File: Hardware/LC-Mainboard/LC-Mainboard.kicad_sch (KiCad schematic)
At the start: 15 parts

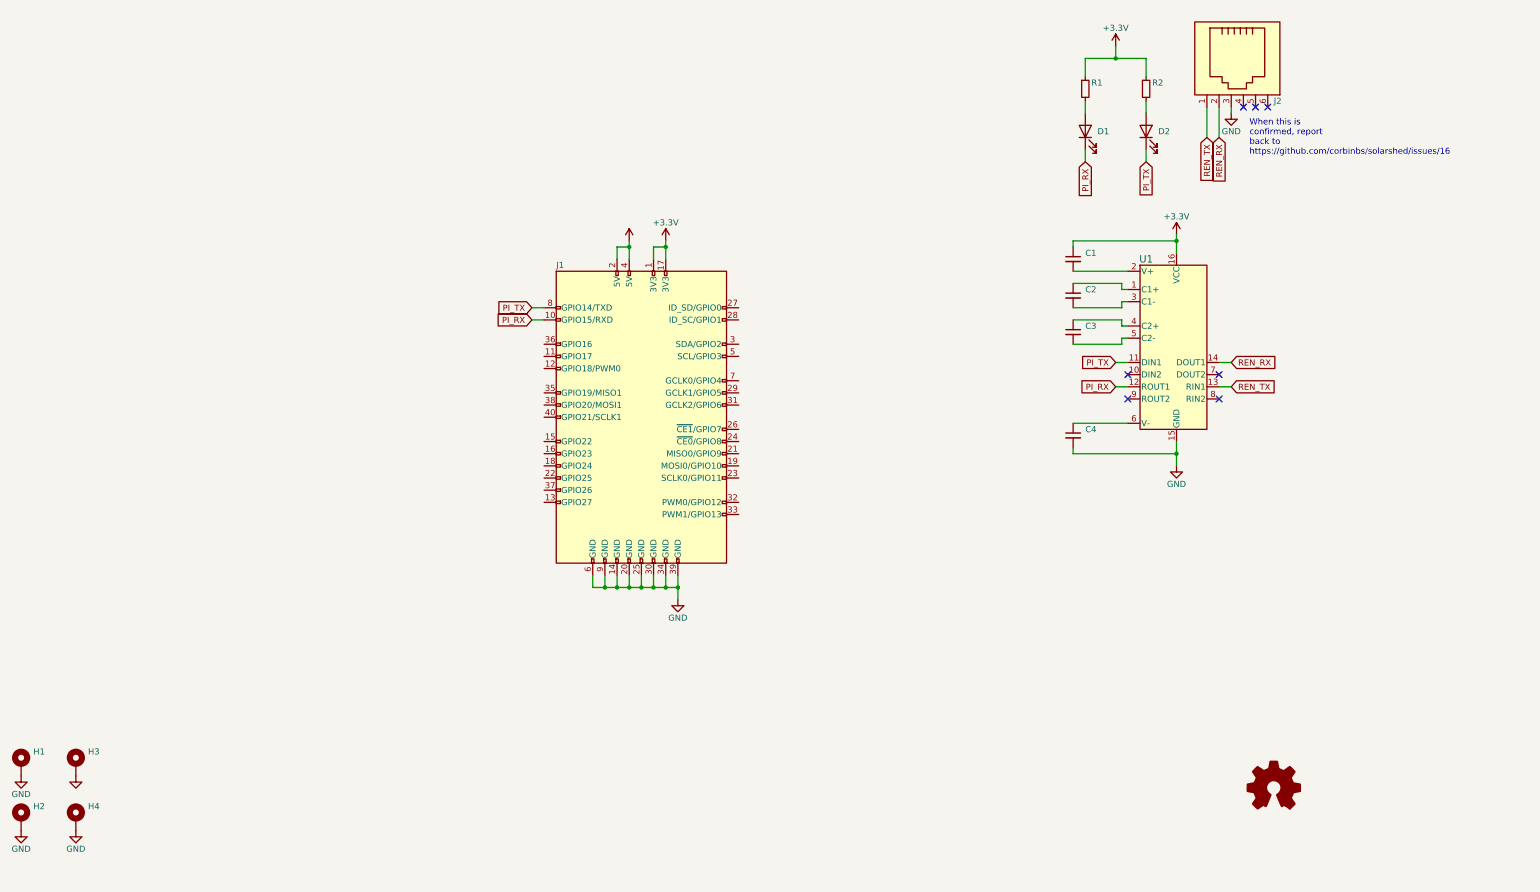
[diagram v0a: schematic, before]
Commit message: Crawler Hardware (#1)
This boilerplates all the hardware, a new branch should be made for producing a v0.1
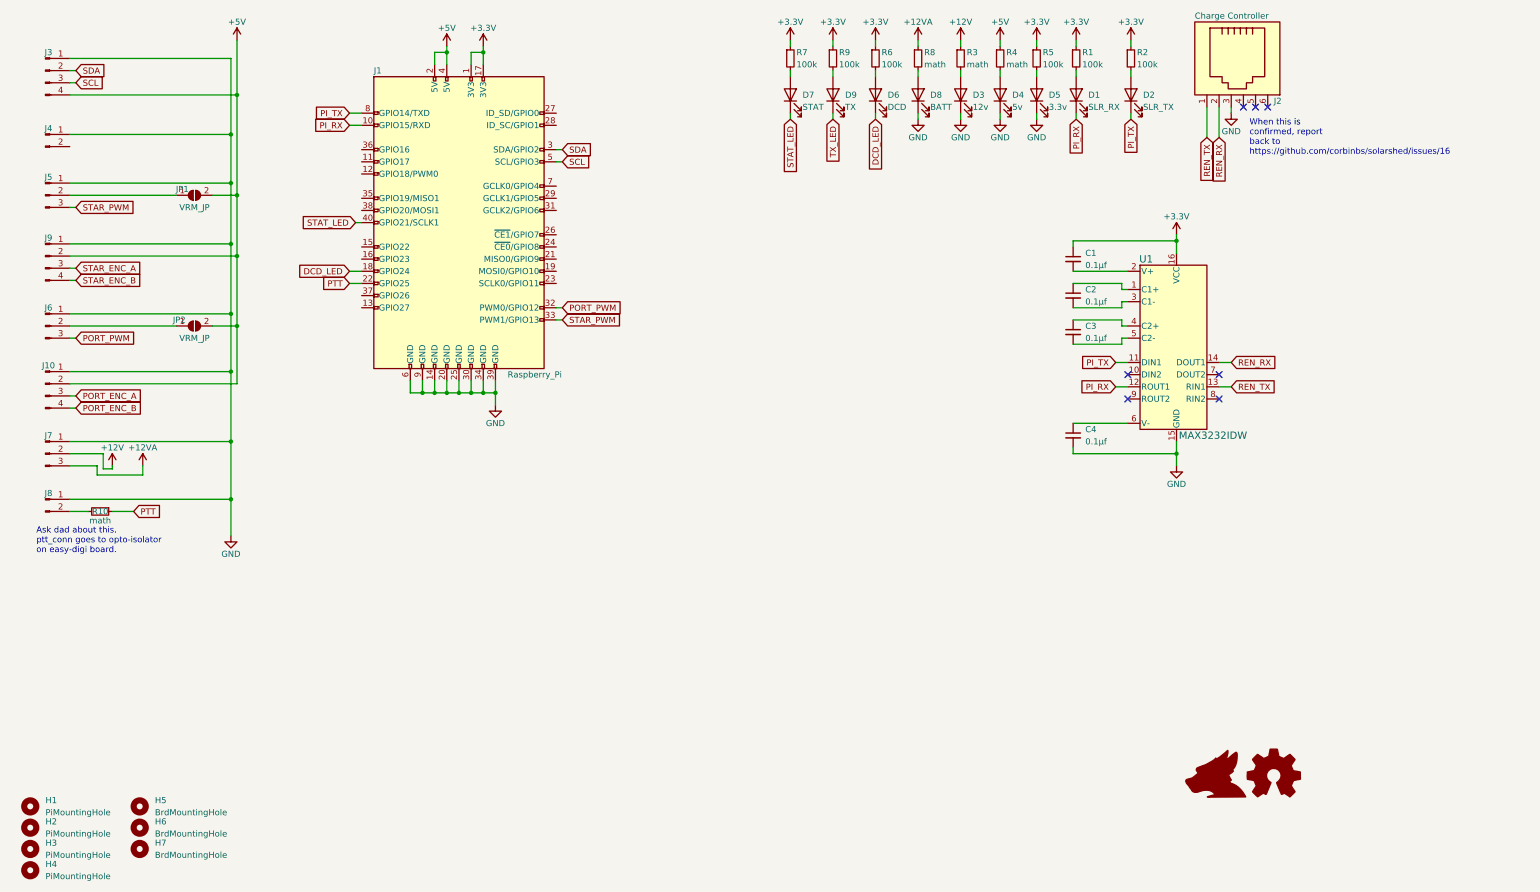
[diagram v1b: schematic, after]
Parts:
- removed H1, H2, H3, H4: (no value), symbol Mechanical:MountingHole_Pad
- added D3: 12v, LED_SMD:LED_0805_2012Metric, symbol Device:LED
- added D4: 5v, LED_SMD:LED_0805_2012Metric, symbol Device:LED
- added D5: 3.3v, LED_SMD:LED_0805_2012Metric, symbol Device:LED
- added D6: DCD, LED_SMD:LED_0805_2012Metric, symbol Device:LED
- added D7: STAT, LED_SMD:LED_0805_2012Metric, symbol Device:LED
- added D8: BATT, LED_SMD:LED_0805_2012Metric, symbol Device:LED
- added D9: TX, LED_SMD:LED_0805_2012Metric, symbol Device:LED
- added H1, H2, H3, H4: PiMountingHole, MountingHole:MountingHole_3mm, symbol Mechanical:MountingHole
- added H5, H6, H7: BrdMountingHole, MountingHole:MountingHole_3mm, symbol Mechanical:MountingHole
- added J10, J3, J9: (no value), Connector_JST:JST_EH_S4B-EH_1x04_P2.50mm_Horizontal, symbol Connector:Conn_01x04_Male
- added J4, J8: (no value), Connector_JST:JST_EH_S2B-EH_1x02_P2.50mm_Horizontal, symbol Connector:Conn_01x02_Male
- added J5, J6, J7: (no value), Connector_JST:JST_EH_S3B-EH_1x03_P2.50mm_Horizontal, symbol Connector:Conn_01x03_Male
- added JP1, JP2: VRM_JP, Jumper:SolderJumper-2_P1.3mm_Open_Pad1.0x1.5mm, symbol Jumper:SolderJumper_2_Open
- added R10, R3, R4, R8: math, Resistor_SMD:R_0805_2012Metric, symbol Device:R_Small
- added R5, R6, R7, R9: 100k, Resistor_SMD:R_0805_2012Metric, symbol Device:R_Small
- C1, C2, C3, C4: value (none) -> 0.1μf; footprint (none) -> Capacitor_SMD:C_0805_2012Metric
- D1: value (none) -> SLR_RX; footprint (none) -> LED_SMD:LED_0805_2012Metric
- D2: value (none) -> SLR_TX; footprint (none) -> LED_SMD:LED_0805_2012Metric
- J1: value (none) -> Raspberry_Pi; footprint (none) -> Connector_PinSocket_2.54mm:PinSocket_2x20_P2.54mm_Vertical
- J2: value (none) -> Charge Controller; footprint (none) -> Connector_RJ:RJ12_Amphenol_54601
- R1, R2: value (none) -> 100k; footprint (none) -> Resistor_SMD:R_0805_2012Metric
- U1: value (none) -> MAX3232IDW; footprint (none) -> KenwoodFox:MAX3232IDW
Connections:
- net +3V3: now also R5.1, R6.1, R7.1, R9.1
- net +5V: now also J10.2 (Pin_2), J3.4 (Pin_4), J9.2 (Pin_2), JP1.2 (B), JP2.2 (B), R4.1
- net GND: now also D3.1 (K), D4.1 (K), D5.1 (K), D8.1 (K), J10.1 (Pin_1), J3.1 (Pin_1), J4.1 (Pin_1), J5.1 (Pin_1), J6.1 (Pin_1), J7.1 (Pin_1), J8.1 (Pin_1), J9.1 (Pin_1)
- net DCD_LED: now reaches J1.18 (GPIO24)
- net DCD_LED: now also D6.1 (K)
- net PTT: now reaches J1.22 (GPIO25)
- net PTT: now also R10.1
- net SDA: now reaches J1.3 (SDA/GPIO2)
- net SDA: now also J3.2 (Pin_2)
- net PORT_PWM: now reaches J1.32 (PWM0/GPIO12)
- net PORT_PWM: now also J6.3 (Pin_3)
- net STAR_PWM: now reaches J1.33 (PWM1/GPIO13)
- net STAR_PWM: now also J5.3 (Pin_3)
- net STAT_LED: now reaches J1.40 (GPIO21/SCLK1)
- net STAT_LED: now also D7.1 (K)
- net SCL: now reaches J1.5 (SCL/GPIO3)
- net SCL: now also J3.3 (Pin_3)
- new net: D6.2 (A), R6.2
- new net: D7.2 (A), R7.2
- new net: J5.2 (Pin_2), JP1.1 (A)
- new net: J8.2 (Pin_2), R10.2
- new net: D8.2 (A), R8.2
- new net: D9.2 (A), R9.2
- new net: D5.2 (A), R5.2
- new net: D3.2 (A), R3.2
- new net: D4.2 (A), R4.2
- new net: J6.2 (Pin_2), JP2.1 (A)
- new net +12V: J7.2 (Pin_2), R3.1
- new net +12VA: J7.3 (Pin_3), R8.1
- new net PORT_ENC_A: J10.3 (Pin_3)
- new net PORT_ENC_B: J10.4 (Pin_4)
- new net STAR_ENC_A: J9.3 (Pin_3)
- new net STAR_ENC_B: J9.4 (Pin_4)
- new net TX_LED: D9.1 (K)
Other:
- note added: "Ask dad about this. ptt_conn goes to opto-isolator on easy-digi board."
- moved on the sheet: D1, D2, J1, R1, R2

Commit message: Switch to the correct connectors
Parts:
- J10, J3, J9: footprint Connector_JST:JST_EH_S4B-EH_1x04_P2.50mm_Horizontal -> (none)
- J4, J8: footprint Connector_JST:JST_EH_S2B-EH_1x02_P2.50mm_Horizontal -> (none)
- J5, J6, J7: footprint Connector_JST:JST_EH_S3B-EH_1x03_P2.50mm_Horizontal -> (none)
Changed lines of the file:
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@@
     (property "Reference" "J3" (id 0) (at 22.225 21.59 0))
     (property "Value" "" (id 1) (at 21.59 32.385 0))
-    (property "Footprint" "Connector_JST:JST_EH_S4B-EH_1x04_P2.50mm_Horizontal" (id 2) (at 21.59 25.4 0)
+    (property "Footprint" "" (id 2) (at 21.59 25.4 0)
       (effects (font (size 1.27 1.27)) hide)
     )
@@
     (property "Reference" "J5" (id 0) (at 22.225 47.625 0))
     (property "Value" "" (id 1) (at 21.59 55.88 0))
-    (property "Footprint" "Connector_JST:JST_EH_S3B-EH_1x03_P2.50mm_Horizontal" (id 2) (at 21.59 51.435 0)
+    (property "Footprint" "" (id 2) (at 21.59 51.435 0)
       (effects (font (size 1.27 1.27)) hide)
     )
@@
     (property "Reference" "J8" (id 0) (at 22.225 113.665 0))
     (property "Value" "" (id 1) (at 22.225 118.745 0))
-    (property "Footprint" "Connector_JST:JST_EH_S2B-EH_1x02_P2.50mm_Horizontal" (id 2) (at 21.59 114.935 0)
+    (property "Footprint" "" (id 2) (at 21.59 114.935 0)
       (effects (font (size 1.27 1.27)) hide)
     )
@@
     (property "Reference" "J10" (id 0) (at 22.225 86.995 0))
     (property "Value" "" (id 1) (at 21.59 97.155 0))
-    (property "Footprint" "Connector_JST:JST_EH_S4B-EH_1x04_P2.50mm_Horizontal" (id 2) (at 21.59 90.805 0)
+    (property "Footprint" "" (id 2) (at 21.59 90.805 0)
       (effects (font (size 1.27 1.27)) hide)
     )
@@
     (property "Reference" "J4" (id 0) (at 22.225 37.465 0))
     (property "Value" "" (id 1) (at 21.59 42.545 0))
-    (property "Footprint" "Connector_JST:JST_EH_S2B-EH_1x02_P2.50mm_Horizontal" (id 2) (at 21.59 38.735 0)
+    (property "Footprint" "" (id 2) (at 21.59 38.735 0)
       (effects (font (size 1.27 1.27)) hide)
     )
@@
     (property "Reference" "J6" (id 0) (at 22.225 74.93 0))
     (property "Value" "" (id 1) (at 21.59 83.185 0))
-    (property "Footprint" "Connector_JST:JST_EH_S3B-EH_1x03_P2.50mm_Horizontal" (id 2) (at 21.59 78.74 0)
+    (property "Footprint" "" (id 2) (at 21.59 78.74 0)
       (effects (font (size 1.27 1.27)) hide)
     )
@@
     (property "Reference" "J7" (id 0) (at 22.225 101.6 0))
     (property "Value" "" (id 1) (at 21.59 109.855 0))
-    (property "Footprint" "Connector_JST:JST_EH_S3B-EH_1x03_P2.50mm_Horizontal" (id 2) (at 21.59 105.41 0)
+    (property "Footprint" "" (id 2) (at 21.59 105.41 0)
       (effects (font (size 1.27 1.27)) hide)
     )
@@
     (property "Reference" "J9" (id 0) (at 22.225 60.325 0))
     (property "Value" "" (id 1) (at 21.59 70.485 0))
-    (property "Footprint" "Connector_JST:JST_EH_S4B-EH_1x04_P2.50mm_Horizontal" (id 2) (at 21.59 64.135 0)
+    (property "Footprint" "" (id 2) (at 21.59 64.135 0)
       (effects (font (size 1.27 1.27)) hide)
     )
@@
     )
     (path "/24476caa-fdcb-4197-9bfb-392c6a073e43"
-      (reference "J3") (unit 1) (value "I²C") (footprint "Connector_JST:JST_EH_S4B-EH_1x04_P2.50mm_Horizontal")
+      (reference "J3") (unit 1) (value "I²C") (footprint "Connector_JST:JST_XH_S4B-XH-A_1x04_P2.50mm_Horizontal")
     )
     (path "/9d5c2274-b455-4ffd-92d8-2c44b26b0be2"
-      (reference "J4") (unit 1) (value "Beacon") (footprint "Connector_JST:JST_EH_S2B-EH_1x02_P2.50mm_Horizontal")
+      (reference "J4") (unit 1) (value "Beacon") (footprint "Connector_JST:JST_XH_S2B-XH-A_1x02_P2.50mm_Horizontal")
     )
     (path "/2608735e-453b-4d6b-8ef9-fb985eff7850"
-      (reference "J5") (unit 1) (value "Star.Motor") (footprint "Connector_JST:JST_EH_S3B-EH_1x03_P2.50mm_Horizontal")
+      (reference "J5") (unit 1) (value "Star.Motor") (footprint "Connector_JST:JST_XH_S3B-XH-A_1x03_P2.50mm_Horizontal")
     )
     (path "/ae944667-42b2-4982-b030-0409ac819ee8"
-      (reference "J6") (unit 1) (value "Port Motor") (footprint "Connector_JST:JST_EH_S3B-EH_1x03_P2.50mm_Horizontal")
+      (reference "J6") (unit 1) (value "Port Motor") (footprint "Connector_JST:JST_XH_S3B-XH-A_1x03_P2.50mm_Horizontal")
     )
     (path "/ccb34e09-657a-42d2-a025-277016b9bdee"
-      (reference "J7") (unit 1) (value "DC In") (footprint "Connector_JST:JST_EH_S3B-EH_1x03_P2.50mm_Horizontal")
+      (reference "J7") (unit 1) (value "DC In") (footprint "Connector_JST:JST_XH_S3B-XH-A_1x03_P2.50mm_Horizontal")
     )
     (path "/3ee0f43d-b1cb-4b41-84f9-e0336f3b41ab"
-      (reference "J8") (unit 1) (value "PTT") (footprint "Connector_JST:JST_EH_S2B-EH_1x02_P2.50mm_Horizontal")
+      (reference "J8") (unit 1) (value "PTT") (footprint "Connector_JST:JST_XH_S2B-XH-A_1x02_P2.50mm_Horizontal")
     )
     (path "/d4f1a31e-04c2-4acf-9b71-d68e437dd209"
-      (reference "J9") (unit 1) (value "Star.Enc.") (footprint "Connector_JST:JST_EH_S4B-EH_1x04_P2.50mm_Horizontal")
+      (reference "J9") (unit 1) (value "Star.Enc.") (footprint "Connector_JST:JST_XH_S4B-XH-A_1x04_P2.50mm_Horizontal")
     )
     (path "/5fa901e5-036a-40bb-8fac-37fc1e656a0b"
-      (reference "J10") (unit 1) (value "Port Enc.") (footprint "Connector_JST:JST_EH_S4B-EH_1x04_P2.50mm_Horizontal")
+      (reference "J10") (unit 1) (value "Port Enc.") (footprint "Connector_JST:JST_XH_S4B-XH-A_1x04_P2.50mm_Horizontal")
     )
     (path "/37968072-4120-49c3-82bc-30739e257550"
